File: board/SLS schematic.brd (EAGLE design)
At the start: 100 x 80 mm, 8 parts, among them IC1 78L05Z, T1 BC848, U1 ATTINY85-20PU

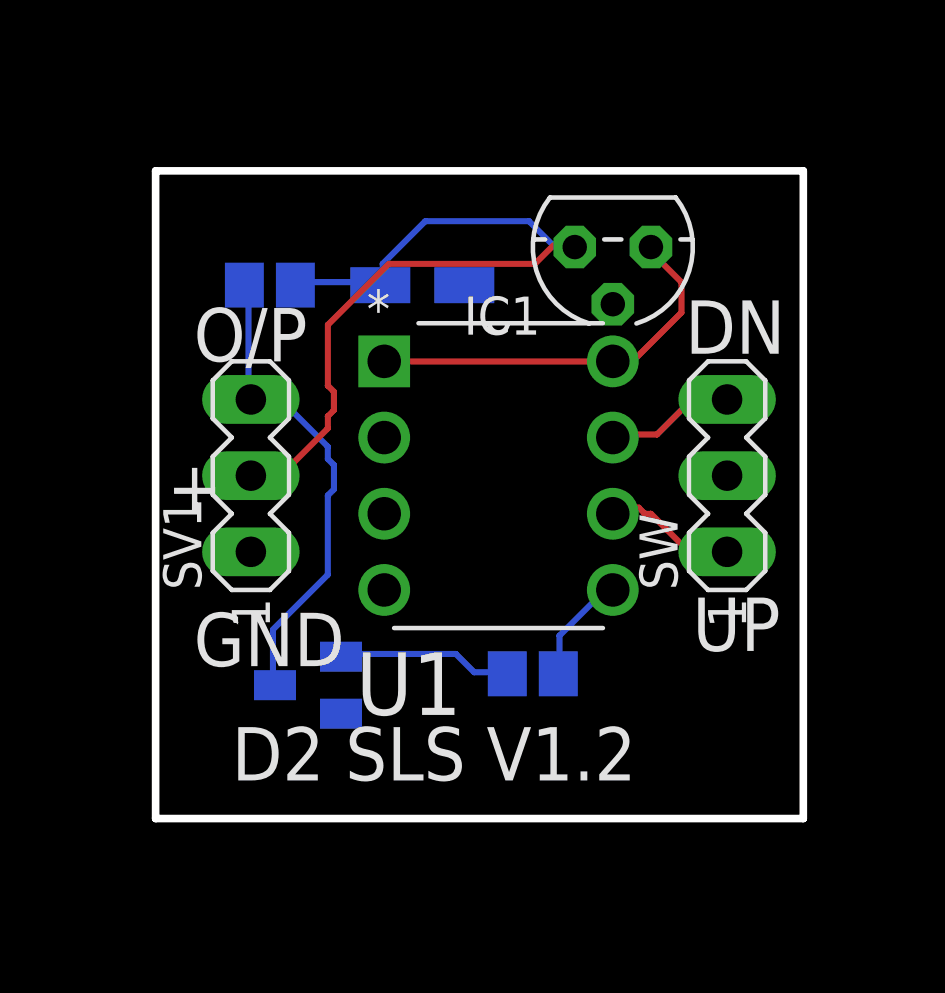
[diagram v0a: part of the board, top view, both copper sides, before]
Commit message: Update to 1.3 v board (untested)
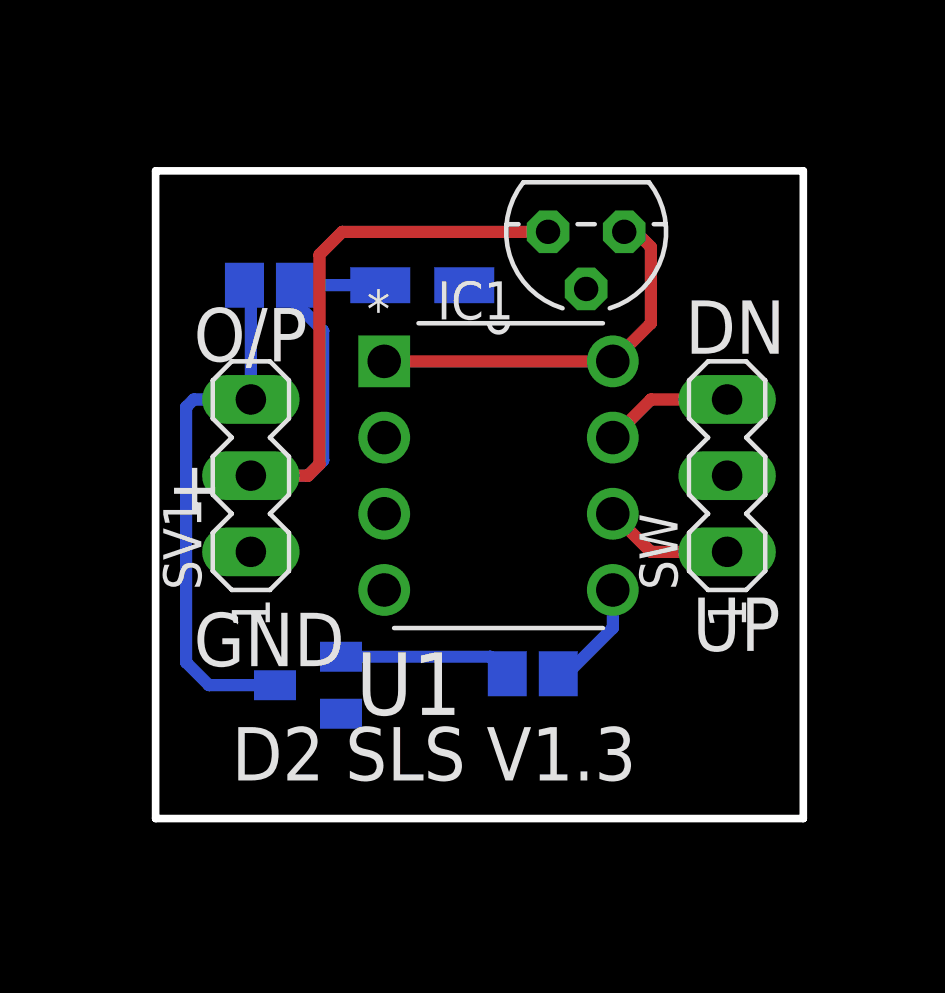
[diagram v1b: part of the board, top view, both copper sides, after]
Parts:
- moved IC1 1.02 mm to (58.8, 50.0)
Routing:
- net 12VOP: track 16.1 -> 18.0 mm
- net 12V: track 27.2 -> 29.0 mm
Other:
- board text added: "D2 SLS V1.3"
- board text removed: "D2 SLS V1.2"
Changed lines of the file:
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@@
 <?xml version="1.0" encoding="utf-8"?>
 <!DOCTYPE eagle SYSTEM "eagle.dtd">
-<eagle version="7.1.0">
+<eagle version="7.6.0">
 <drawing>
 <settings>
@@
 <wire x1="66.04" y1="30.48" x2="66.04" y2="52.07" width="0.254" layer="20"/>
 <wire x1="66.04" y1="52.07" x2="44.45" y2="52.07" width="0.254" layer="20"/>
-<text x="46.99" y="31.75" size="1.778" layer="21" font="vector" ratio="15">D2 SLS V1.2</text>
+<text x="46.99" y="31.75" size="1.778" layer="21" font="vector" ratio="15">D2 SLS V1.3</text>
 <text x="58.42" y="33.02" size="1.27" layer="22" font="vector" ratio="15" rot="MR0">3K</text>
 <text x="48.641" y="49.53" size="1.27" layer="22" font="vector" ratio="15" rot="MR0">1K</text>
@@
 </autorouter>
 <elements>
-<element name="IC1" library="linear" package="TO92" value="78L05Z" x="59.69" y="49.53" rot="R180"/>
+<element name="IC1" library="linear" package="TO92" value="78L05Z" x="58.801" y="50.038" rot="R180"/>
 <element name="R1" library="resistor" package="R0805" value="" x="57.023" y="35.306" rot="MR180">
 <attribute name="SPICEPREFIX" value="R" x="57.023" y="35.306" size="1.778" layer="28" rot="MR180" display="off"/>
@@
 <contactref element="U1" pad="8"/>
 <contactref element="U1" pad="1"/>
-<wire x1="61.976" y1="48.3616" x2="60.96" y2="49.3776" width="0.2032" layer="1"/>
-<wire x1="61.976" y1="47.3456" x2="61.976" y2="48.3616" width="0.2032" layer="1"/>
-<wire x1="60.3504" y1="45.72" x2="61.976" y2="47.3456" width="0.2032" layer="1"/>
-<wire x1="59.69" y1="45.72" x2="60.3504" y2="45.72" width="0.2032" layer="1"/>
-<wire x1="60.96" y1="49.3776" x2="60.96" y2="49.53" width="0.2032" layer="1"/>
-<wire x1="59.69" y1="45.72" x2="52.07" y2="45.72" width="0.2032" layer="1"/>
+<wire x1="59.69" y1="45.72" x2="52.07" y2="45.72" width="0.4064" layer="1"/>
+<wire x1="60.071" y1="50.038" x2="60.452" y2="50.038" width="0.4064" layer="1"/>
+<wire x1="60.452" y1="50.038" x2="60.96" y2="49.53" width="0.4064" layer="1"/>
+<wire x1="60.96" y1="49.53" x2="60.96" y2="46.99" width="0.4064" layer="1"/>
+<wire x1="60.96" y1="46.99" x2="59.69" y2="45.72" width="0.4064" layer="1"/>
 </signal>
 <signal name="N$2">
 <contactref element="T1" pad="1"/>
 <contactref element="R1" pad="1"/>
-<wire x1="54.4576" y1="35.9664" x2="50.8" y2="35.9664" width="0.2032" layer="16"/>
-<wire x1="55.0672" y1="35.3568" x2="54.4576" y2="35.9664" width="0.2032" layer="16"/>
-<wire x1="56.0832" y1="35.3568" x2="55.0672" y2="35.3568" width="0.2032" layer="16"/>
-<wire x1="50.8" y1="35.9664" x2="50.63" y2="35.875" width="0.2032" layer="16"/>
-<wire x1="56.0832" y1="35.3568" x2="56.173" y2="35.306" width="0.2032" layer="16"/>
+<wire x1="50.63" y1="35.875" x2="55.604" y2="35.875" width="0.4064" layer="16"/>
+<wire x1="55.604" y1="35.875" x2="56.173" y2="35.306" width="0.4064" layer="16"/>
 </signal>
 <signal name="O/P">
 <contactref element="U1" pad="5"/>
 <contactref element="R1" pad="2"/>
-<wire x1="59.5376" y1="38.2016" x2="57.912" y2="36.576" width="0.2032" layer="16"/>
-<wire x1="59.5376" y1="38.2016" x2="59.69" y2="38.1" width="0.2032" layer="16"/>
-<wire x1="57.912" y1="36.576" x2="57.912" y2="35.3568" width="0.2032" layer="16"/>
-<wire x1="57.912" y1="35.3568" x2="57.873" y2="35.306" width="0.2032" layer="16"/>
+<wire x1="57.873" y1="35.306" x2="58.166" y2="35.306" width="0.4064" layer="16"/>
+<wire x1="58.166" y1="35.306" x2="59.69" y2="36.83" width="0.4064" layer="16"/>
+<wire x1="59.69" y1="36.83" x2="59.69" y2="38.1" width="0.4064" layer="16"/>
 </signal>
 <signal name="UP">
 <contactref element="U1" pad="6"/>
 <contactref element="SW" pad="1"/>
-<wire x1="62.1792" y1="39.4208" x2="63.3984" y2="39.4208" width="0.2032" layer="1"/>
-<wire x1="60.96" y1="40.64" x2="62.1792" y2="39.4208" width="0.2032" layer="1"/>
-<wire x1="60.7568" y1="40.64" x2="60.96" y2="40.64" width="0.2032" layer="1"/>
-<wire x1="60.5536" y1="40.8432" x2="60.7568" y2="40.64" width="0.2032" layer="1"/>
-<wire x1="59.944" y1="40.8432" x2="60.5536" y2="40.8432" width="0.2032" layer="1"/>
-<wire x1="59.7408" y1="40.64" x2="59.944" y2="40.8432" width="0.2032" layer="1"/>
-<wire x1="63.3984" y1="39.4208" x2="63.5" y2="39.37" width="0.2032" layer="1"/>
-<wire x1="59.7408" y1="40.64" x2="59.69" y2="40.64" width="0.2032" layer="1"/>
+<wire x1="59.69" y1="40.64" x2="60.96" y2="39.37" width="0.4064" layer="1"/>
+<wire x1="60.96" y1="39.37" x2="63.5" y2="39.37" width="0.4064" layer="1"/>
 </signal>
 <signal name="12V">
@@
 <contactref element="C1" pad="+"/>
 <contactref element="R2" pad="1"/>
-<wire x1="51.816" y1="48.3616" x2="49.1744" y2="48.3616" width="0.2032" layer="16"/>
-<wire x1="49.1744" y1="48.3616" x2="49.11" y2="48.26" width="0.2032" layer="16"/>
-<wire x1="51.816" y1="48.3616" x2="51.94" y2="48.26" width="0.2032" layer="16"/>
-<wire x1="52.0192" y1="48.9712" x2="52.0192" y2="48.3616" width="0.2032" layer="16"/>
-<wire x1="53.4416" y1="50.3936" x2="52.0192" y2="48.9712" width="0.2032" layer="16"/>
-<wire x1="56.896" y1="50.3936" x2="53.4416" y2="50.3936" width="0.2032" layer="16"/>
-<wire x1="57.7088" y1="49.5808" x2="56.896" y2="50.3936" width="0.2032" layer="16"/>
-<wire x1="58.3184" y1="49.5808" x2="57.7088" y2="49.5808" width="0.2032" layer="16"/>
-<wire x1="52.0192" y1="48.3616" x2="51.94" y2="48.26" width="0.2032" layer="16"/>
-<wire x1="58.3184" y1="49.5808" x2="58.42" y2="49.53" width="0.2032" layer="16"/>
-<wire x1="48.768" y1="42.0624" x2="47.752" y2="42.0624" width="0.2032" layer="1"/>
-<wire x1="50.1904" y1="43.4848" x2="48.768" y2="42.0624" width="0.2032" layer="1"/>
-<wire x1="50.1904" y1="43.8912" x2="50.1904" y2="43.4848" width="0.2032" layer="1"/>
-<wire x1="50.3936" y1="44.0944" x2="50.1904" y2="43.8912" width="0.2032" layer="1"/>
-<wire x1="50.3936" y1="44.704" x2="50.3936" y2="44.0944" width="0.2032" layer="1"/>
-<wire x1="50.1904" y1="44.9072" x2="50.3936" y2="44.704" width="0.2032" layer="1"/>
-<wire x1="50.1904" y1="46.9392" x2="50.1904" y2="44.9072" width="0.2032" layer="1"/>
-<wire x1="52.2224" y1="48.9712" x2="50.1904" y2="46.9392" width="0.2032" layer="1"/>
-<wire x1="57.0992" y1="48.9712" x2="52.2224" y2="48.9712" width="0.2032" layer="1"/>
-<wire x1="57.7088" y1="49.5808" x2="57.0992" y2="48.9712" width="0.2032" layer="1"/>
-<wire x1="58.3184" y1="49.5808" x2="57.7088" y2="49.5808" width="0.2032" layer="1"/>
-<wire x1="47.752" y1="42.0624" x2="47.625" y2="41.91" width="0.2032" layer="1"/>
-<wire x1="58.3184" y1="49.5808" x2="58.42" y2="49.53" width="0.2032" layer="1"/>
+<wire x1="49.11" y1="48.26" x2="51.94" y2="48.26" width="0.4064" layer="16"/>
+<wire x1="49.11" y1="48.26" x2="49.11" y2="47.664" width="0.4064" layer="16"/>
+<wire x1="49.11" y1="47.664" x2="50.038" y2="46.736" width="0.4064" layer="16"/>
+<wire x1="50.038" y1="46.736" x2="50.038" y2="42.418" width="0.4064" layer="16"/>
+<wire x1="50.038" y1="42.418" x2="49.53" y2="41.91" width="0.4064" layer="16"/>
+<wire x1="49.53" y1="41.91" x2="47.625" y2="41.91" width="0.4064" layer="16"/>
+<wire x1="57.531" y1="50.038" x2="50.673" y2="50.038" width="0.4064" layer="1"/>
+<wire x1="50.673" y1="50.038" x2="49.911" y2="49.276" width="0.4064" layer="1"/>
+<wire x1="49.911" y1="49.276" x2="49.911" y2="42.291" width="0.4064" layer="1"/>
+<wire x1="49.911" y1="42.291" x2="49.53" y2="41.91" width="0.4064" layer="1"/>
+<wire x1="49.53" y1="41.91" x2="47.625" y2="41.91" width="0.4064" layer="1"/>
 </signal>
 <signal name="GND">
@@
 <contactref element="SW" pad="3"/>
 <contactref element="U1" pad="7"/>
-<wire x1="62.1792" y1="44.2976" x2="63.3984" y2="44.2976" width="0.2032" layer="1"/>
-<wire x1="61.1632" y1="43.2816" x2="62.1792" y2="44.2976" width="0.2032" layer="1"/>
-<wire x1="59.7408" y1="43.2816" x2="61.1632" y2="43.2816" width="0.2032" layer="1"/>
-<wire x1="63.3984" y1="44.2976" x2="63.5" y2="44.45" width="0.2032" layer="1"/>
-<wire x1="59.7408" y1="43.2816" x2="59.69" y2="43.18" width="0.2032" layer="1"/>
+<wire x1="63.5" y1="44.45" x2="60.96" y2="44.45" width="0.4064" layer="1"/>
+<wire x1="60.96" y1="44.45" x2="59.69" y2="43.18" width="0.4064" layer="1"/>
 </signal>
 <signal name="12VOP">
@@
 <contactref element="SV1" pad="3"/>
 <contactref element="R2" pad="2"/>
-<wire x1="48.3616" y1="36.7792" x2="48.3616" y2="34.9504" width="0.2032" layer="16"/>
-<wire x1="50.1904" y1="38.608" x2="48.3616" y2="36.7792" width="0.2032" layer="16"/>
-<wire x1="50.1904" y1="41.2496" x2="50.1904" y2="38.608" width="0.2032" layer="16"/>
-<wire x1="50.3936" y1="41.4528" x2="50.1904" y2="41.2496" width="0.2032" layer="16"/>
-<wire x1="50.3936" y1="42.2656" x2="50.3936" y2="41.4528" width="0.2032" layer="16"/>
-<wire x1="50.1904" y1="42.4688" x2="50.3936" y2="42.2656" width="0.2032" layer="16"/>
-<wire x1="50.1904" y1="42.8752" x2="50.1904" y2="42.4688" width="0.2032" layer="16"/>
-<wire x1="48.768" y1="44.2976" x2="50.1904" y2="42.8752" width="0.2032" layer="16"/>
-<wire x1="47.752" y1="44.2976" x2="48.768" y2="44.2976" width="0.2032" layer="16"/>
-<wire x1="48.3616" y1="34.9504" x2="48.43" y2="34.925" width="0.2032" layer="16"/>
-<wire x1="47.752" y1="44.2976" x2="47.625" y2="44.45" width="0.2032" layer="16"/>
-<wire x1="47.5488" y1="44.5008" x2="47.5488" y2="48.1584" width="0.2032" layer="16"/>
-<wire x1="47.5488" y1="48.1584" x2="47.41" y2="48.26" width="0.2032" layer="16"/>
-<wire x1="47.5488" y1="44.5008" x2="47.625" y2="44.45" width="0.2032" layer="16"/>
+<wire x1="47.625" y1="44.45" x2="47.625" y2="48.045" width="0.4064" layer="16"/>
+<wire x1="47.625" y1="48.045" x2="47.41" y2="48.26" width="0.4064" layer="16"/>
+<wire x1="48.43" y1="34.925" x2="46.228" y2="34.925" width="0.4064" layer="16"/>
+<wire x1="46.228" y1="34.925" x2="45.466" y2="35.687" width="0.4064" layer="16"/>
+<wire x1="45.466" y1="35.687" x2="45.466" y2="44.196" width="0.4064" layer="16"/>
+<wire x1="45.466" y1="44.196" x2="45.72" y2="44.45" width="0.4064" layer="16"/>
+<wire x1="45.72" y1="44.45" x2="47.625" y2="44.45" width="0.4064" layer="16"/>
 </signal>
 </signals>
